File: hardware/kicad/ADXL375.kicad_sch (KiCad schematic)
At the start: 5 parts, among them U401 ADXL375

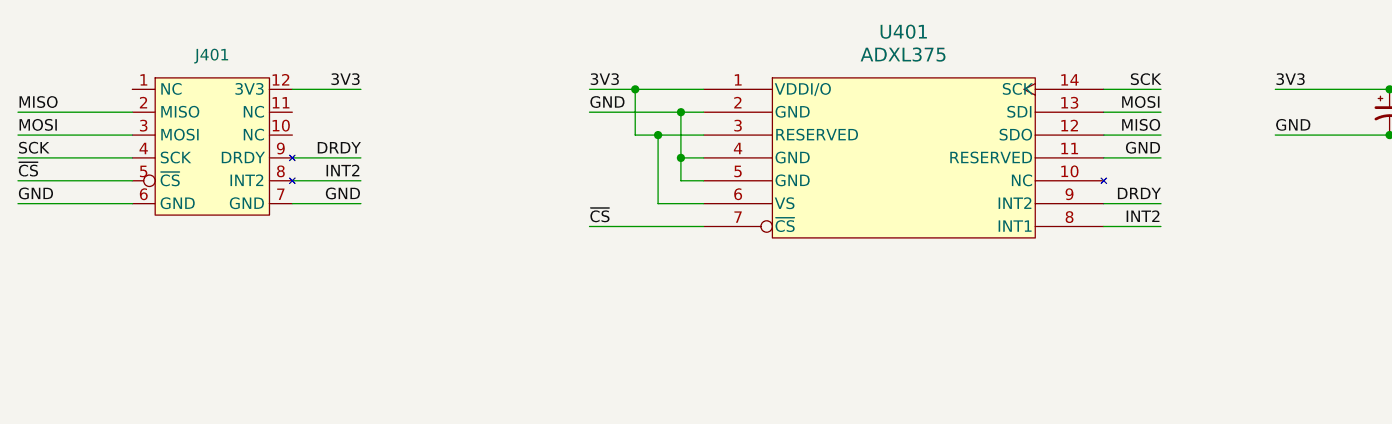
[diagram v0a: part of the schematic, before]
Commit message: Moved sensors from stamp to direct placement
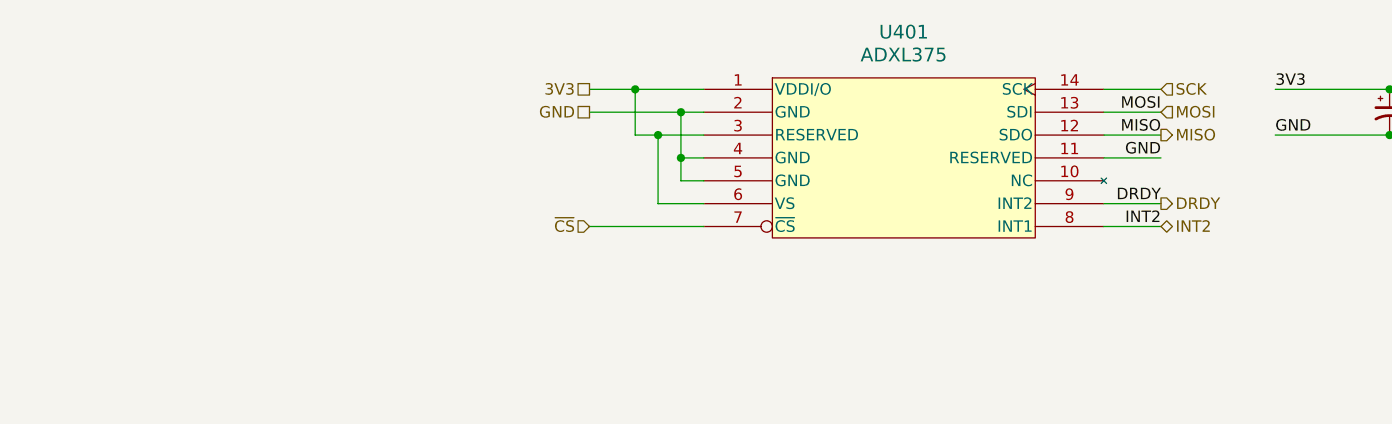
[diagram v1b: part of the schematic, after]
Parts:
- removed J401: (no value), footprints:Stamp, symbol rollercoasterometer2026:STAMP
